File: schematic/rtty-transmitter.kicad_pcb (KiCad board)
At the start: 2 copper layers, 120 x 60 mm, 75 parts, among them J1 USB Type B Connector, J2 USBasp header, J3 2x5 Pin Header Connector Fema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, J4 Conn_01x02_Pin, J5 Conn_01x02_Pin, J6 Conn_01x02_Pin, J7 SMA Vertical Female, Q1 PN2222A, Q2 PN2222A, U1 MCP2221AxP, U2 ATmega328P-P, U3 MCP4901, U4 25LC1024, U5 MCP6022, Y1 16 MHz

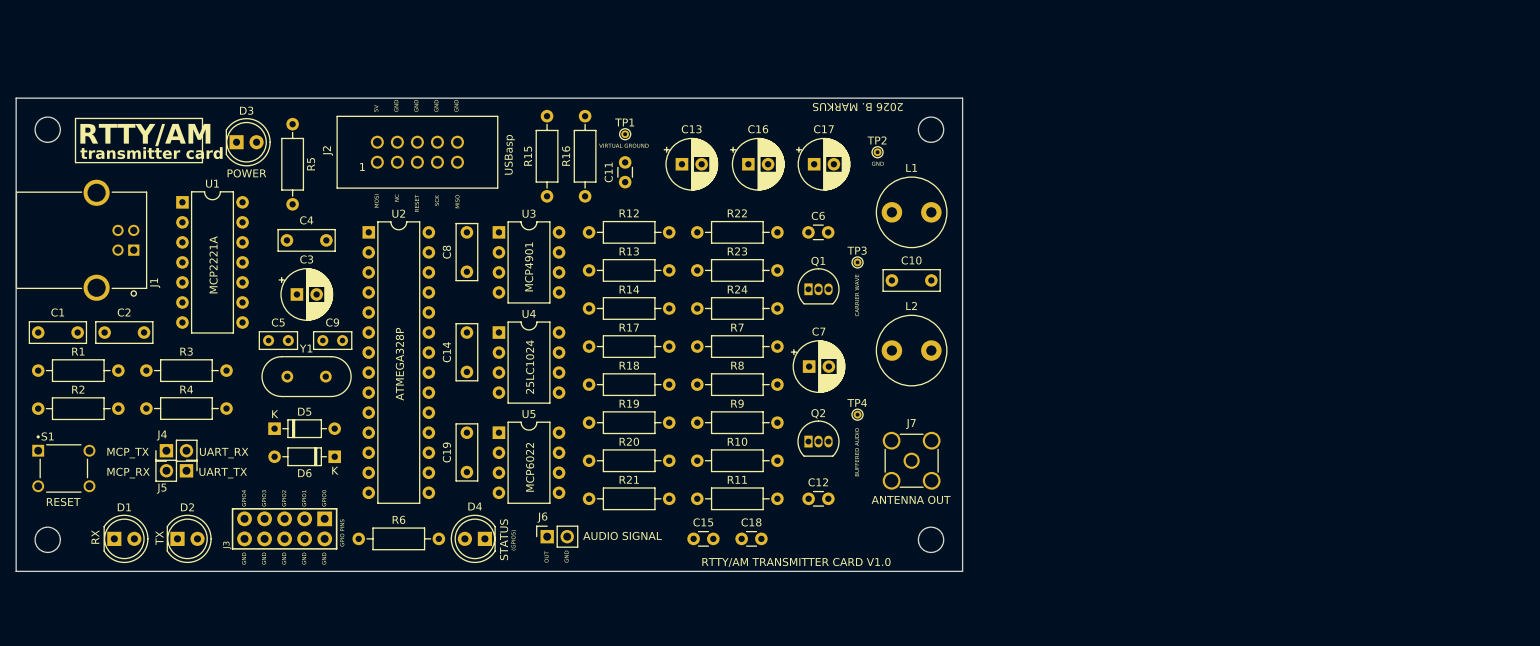
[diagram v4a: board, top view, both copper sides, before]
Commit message: PCB: Ground plane fill zones added
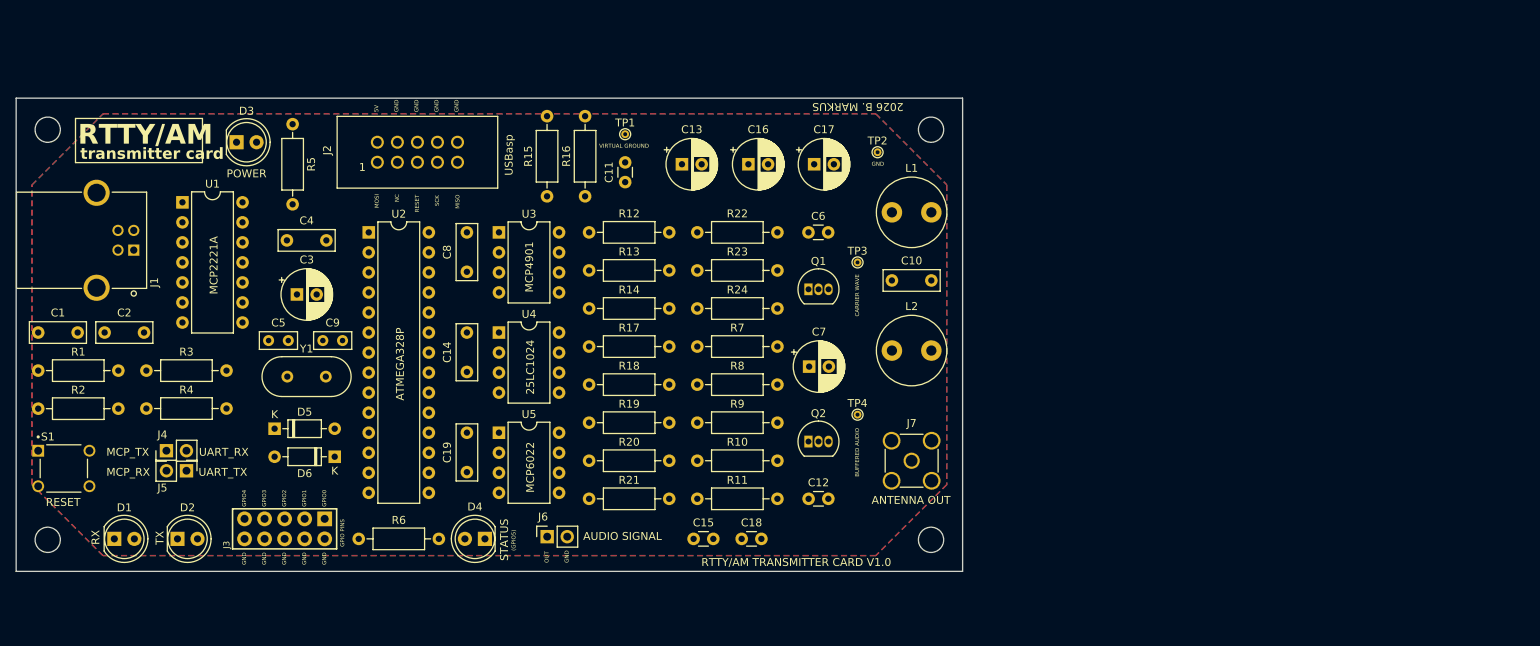
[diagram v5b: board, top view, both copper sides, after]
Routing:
- added copper zone on B.Cu, net GND
- added copper zone on F.Cu, net GND
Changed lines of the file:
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@@
+    )
+  )
+  (zone (net 2) (net_name "GND") (layers "F&B.Cu") (hatch edge 0.5)
+    (connect_pads (clearance 0.5))
+    (min_thickness 0.25) (filled_areas_thickness no)
+    (fill (thermal_gap 0.5) (thermal_bridge_width 0.5))
+    (polygon
+      (pts
+        (xy 2 11)
+        (xy 11 2)
+        (xy 109 2)
+        (xy 118 11)
+        (xy 118 49)
+        (xy 109 58)
+        (xy 11 58)
+        (xy 2 49)
+      )
     )
   )

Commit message: PCB: Routing started
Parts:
- moved C14 5.00 mm to (57.1, 29.7), turned to -90 degrees
- moved C10 5.00 mm to (116.0, 23.1), turned to 180 degrees
- moved C19 5.00 mm to (57.1, 42.4), turned to -90 degrees
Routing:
- net MOSI: track 0.00 -> 69.5 mm
- net Net-(C10-Pad2): track 0.00 -> 32.1 mm
- net SCK: track 0.00 -> 24.2 mm
- net RESET: track 0.00 -> 20.2 mm
- net +5V: track 0.00 -> 19.3 mm
- net Net-(J7-In): track 0.00 -> 15.0 mm
- net Net-(Q1-C): track 0.00 -> 8.64 mm
- net Net-(U2-XTAL1/PB6): track 0.00 -> 5.56 mm
- net Net-(U2-XTAL2/PB7): track 0.00 -> 4.73 mm
- net Net-(D5-K): track 0.00 -> 3.56 mm
- net Net-(D5-A): track 0.00 -> 3.56 mm
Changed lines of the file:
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@@
   )
   (footprint "StockLib:C_100nF_L7.0mm_W2.5mm_P5.00mm" (layer "F.Cu")
-    (at 111.038 23.114)
+    (at 116.038 23.114 180)
     (descr "C, Rect series, Radial, pin pitch=5.00mm, , length*width=7*2.5mm^2, Capacitor")
     (tags "C Rect series Radial pin pitch 5.00mm  length 7mm width 2.5mm Capacitor")
@@
     (property "ki_keywords" "cap capacitor")
     (attr through_hole)
-    (fp_text reference "C10" (at 2.5 -2.5) (layer "F.SilkS")
+    (fp_text reference "C10" (at 2.5 2.54) (layer "F.SilkS")
         (effects (font (size 1 1) (thickness 0.15)))
     )
@@
     (fp_line (start 6 1.25) (end 6 -1.25)
       (stroke (width 0.1) (type solid)) (layer "F.Fab"))
-    (pad "1" thru_hole circle (at 0 0) (size 1.6 1.6) (drill 0.8) (layers "*.Cu" "*.Mask")
+    (pad "1" thru_hole circle (at 0 0 180) (size 1.6 1.6) (drill 0.8) (layers "*.Cu" "*.Mask")
       (net 36 "Net-(Q1-C)") (pintype "passive"))
-    (pad "2" thru_hole circle (at 5 0) (size 1.6 1.6) (drill 0.8) (layers "*.Cu" "*.Mask")
+    (pad "2" thru_hole circle (at 5 0 180) (size 1.6 1.6) (drill 0.8) (layers "*.Cu" "*.Mask")
       (net 16 "Net-(C10-Pad2)") (pintype "passive"))
     (model "C:/Users/bazsi/Documents/KiCad/7.0/3dmodels/Cap 100nF.step"
@@
   )
   (footprint "StockLib:C_100nF_L7.0mm_W2.5mm_P5.00mm" (layer "F.Cu")
-    (at 57.15 34.718 90)
+    (at 57.15 29.718 -90)
     (descr "C, Rect series, Radial, pin pitch=5.00mm, , length*width=7*2.5mm^2, Capacitor")
     (tags "C Rect series Radial pin pitch 5.00mm  length 7mm width 2.5mm Capacitor")
@@
     (property "ki_keywords" "cap capacitor")
     (attr through_hole)
-    (fp_text reference "C14" (at 2.5 -2.5 90) (layer "F.SilkS")
+    (fp_text reference "C14" (at 2.54 2.54 90) (layer "F.SilkS")
         (effects (font (size 1 1) (thickness 0.15)))
     )
@@
     (fp_line (start 6 1.25) (end 6 -1.25)
       (stroke (width 0.1) (type solid)) (layer "F.Fab"))
-    (pad "1" thru_hole circle (at 0 0 90) (size 1.6 1.6) (drill 0.8) (layers "*.Cu" "*.Mask")
+    (pad "1" thru_hole circle (at 0 0 270) (size 1.6 1.6) (drill 0.8) (layers "*.Cu" "*.Mask")
       (net 5 "+5V") (pintype "passive"))
-    (pad "2" thru_hole circle (at 5 0 90) (size 1.6 1.6) (drill 0.8) (layers "*.Cu" "*.Mask")
+    (pad "2" thru_hole circle (at 5 0 270) (size 1.6 1.6) (drill 0.8) (layers "*.Cu" "*.Mask")
       (net 2 "GND") (pintype "passive"))
     (model "C:/Users/bazsi/Documents/KiCad/7.0/3dmodels/Cap 100nF.step"
@@
   )
   (footprint "StockLib:C_100nF_L7.0mm_W2.5mm_P5.00mm" (layer "F.Cu")
-    (at 57.15 47.418 90)
+    (at 57.15 42.418 -90)
     (descr "C, Rect series, Radial, pin pitch=5.00mm, , length*width=7*2.5mm^2, Capacitor")
     (tags "C Rect series Radial pin pitch 5.00mm  length 7mm width 2.5mm Capacitor")
@@
     (property "ki_keywords" "cap capacitor")
     (attr through_hole)
-    (fp_text reference "C19" (at 2.5 -2.5 90) (layer "F.SilkS")
+    (fp_text reference "C19" (at 2.54 2.54 90) (layer "F.SilkS")
         (effects (font (size 1 1) (thickness 0.15)))
     )
@@
     (fp_line (start 6 1.25) (end 6 -1.25)
       (stroke (width 0.1) (type solid)) (layer "F.Fab"))
-    (pad "1" thru_hole circle (at 0 0 90) (size 1.6 1.6) (drill 0.8) (layers "*.Cu" "*.Mask")
+    (pad "1" thru_hole circle (at 0 0 270) (size 1.6 1.6) (drill 0.8) (layers "*.Cu" "*.Mask")
       (net 5 "+5V") (pintype "passive"))
-    (pad "2" thru_hole circle (at 5 0 90) (size 1.6 1.6) (drill 0.8) (layers "*.Cu" "*.Mask")
+    (pad "2" thru_hole circle (at 5 0 270) (size 1.6 1.6) (drill 0.8) (layers "*.Cu" "*.Mask")
       (net 2 "GND") (pintype "passive"))
     (model "C:/Users/bazsi/Documents/KiCad/7.0/3dmodels/Cap 100nF.step"
@@
     )
   )
+  (segment (start 34.38 35.306) (end 32.004 32.93) (width 0.25) (layer "F.Cu") (net 3))
+  (segment (start 32.004 32.93) (end 32.004 30.734) (width 0.25) (layer "F.Cu") (net 3))
+  (segment (start 39.26 35.306) (end 39.26 31.112) (width 0.25) (layer "F.Cu") (net 4))
+  (segment (start 39.26 31.112) (end 38.882 30.734) (width 0.25) (layer "F.Cu") (net 4))
+  (segment (start 7.62 29.718) (end 7.794 29.718) (width 0.5) (layer "F.Cu") (net 5))
+  (segment (start 14.91 19.27) (end 15.02 19.27) (width 0.5) (layer "F.Cu") (net 5))
+  (segment (start 7.62 39.37) (end 2.794 34.544) (width 0.5) (layer "F.Cu") (net 5))
+  (segment (start 2.794 34.544) (end 7.62 29.718) (width 0.5) (layer "F.Cu") (net 5))
+  (segment (start 12.954 39.37) (end 7.62 39.37) (width 0.5) (layer "F.Cu") (net 5))
+  (segment (start 61.214 24.317009) (end 52.0262 15.129209) (width 0.25) (layer "F.Cu") (net 14))
+  (segment (start 44.879991 23.223) (end 51.054 29.397009) (width 0.25) (layer "F.Cu") (net 14))
+  (segment (start 44.238009 23.223) (end 44.879991 23.223) (width 0.25) (layer "F.Cu") (net 14))
+  (segment (start 51.054 43.688) (end 52.324 44.958) (width 0.25) (layer "F.Cu") (net 14))
+  (segment (start 61.214 24.638) (end 61.214 24.317009) (width 0.25) (layer "F.Cu") (net 14))
+  (segment (start 51.352546 6.978) (end 46.9462 6.978) (width 0.25) (layer "F.Cu") (net 14))
+  (segment (start 43.579 10.3452) (end 43.579 22.563991) (width 0.25) (layer "F.Cu") (net 14))
+  (segment (start 46.9462 6.978) (end 45.7962 8.128) (width 0.25) (layer "F.Cu") (net 14))
+  (segment (start 43.579 22.563991) (end 44.238009 23.223) (width 0.25) (layer "F.Cu") (net 14))
+  (segment (start 45.7962 8.128) (end 43.579 10.3452) (width 0.25) (layer "F.Cu") (net 14))
+  (segment (start 51.054 29.397009) (end 51.054 43.688) (width 0.25) (layer "F.Cu") (net 14))
+  (segment (start 52.0262 15.129209) (end 52.0262 7.651654) (width 0.25) (layer "F.Cu") (net 14))
+  (segment (start 52.0262 7.651654) (end 51.352546 6.978) (width 0.25) (layer "F.Cu") (net 14))
+  (segment (start 3.96 39.37) (end 2.794 39.37) (width 0.25) (layer "F.Cu") (net 15))
+  (segment (start 44.704 14.3002) (end 44.704 17.018) (width 0.25) (layer "F.Cu") (net 15))
+  (segment (start 50.8762 8.128) (end 44.704 14.3002) (width 0.25) (layer "F.Cu") (net 15))
+  (segment (start 9.294 44.704) (end 3.96 39.37) (width 0.25) (layer "F.Cu") (net 15))
+  (segment (start 108.458 34.584) (end 111.038 32.004) (width 0.25) (layer "F.Cu") (net 16))
+  (segment (start 111.038 32.004) (end 111.038 23.114) (width 1) (layer "F.Cu") (net 16))
+  (segment (start 106.319 44.958) (end 106.426 44.958) (width 0.25) (layer "F.Cu") (net 16))
+  (segment (start 108.458 42.926) (end 108.458 34.584) (width 0.25) (layer "F.Cu") (net 16))
+  (segment (start 100.477 50.8) (end 106.319 44.958) (width 0.25) (layer "F.Cu") (net 16))
+  (segment (start 106.426 44.958) (end 108.458 42.926) (width 0.25) (layer "F.Cu") (net 16))
+  (segment (start 53.4162 8.128) (end 54.5662 6.978) (width 0.25) (layer "F.Cu") (net 22))
+  (segment (start 54.5662 6.978) (end 60.826 6.978) (width 0.25) (layer "F.Cu") (net 22))
+  (segment (start 62.484 8.636) (end 62.484 20.828) (width 0.25) (layer "F.Cu") (net 22))
+  (segment (start 62.484 20.828) (end 61.214 22.098) (width 0.25) (layer "F.Cu") (net 22))
+  (segment (start 60.826 6.978) (end 62.484 8.636) (width 0.25) (layer "F.Cu") (net 22))
+  (segment (start 116.038 14.478) (end 116.038 23.114) (width 1) (layer "F.Cu") (net 36))
+  (segment (start 32.766 45.466) (end 32.766 41.91) (width 0.25) (layer "F.Cu") (net 44))
+  (segment (start 40.386 41.91) (end 40.386 45.466) (width 0.25) (layer "F.Cu") (net 45))
+  (segment (start 116.038 32.004) (end 113.538 34.504) (width 1) (layer "F.Cu") (net 46))
+  (segment (start 113.538 34.504) (end 113.538 45.974) (width 1) (layer "F.Cu") (net 46))
   (zone (net 2) (net_name "GND") (layers "F&B.Cu") (hatch edge 0.5)
     (connect_pads (clearance 0.5))

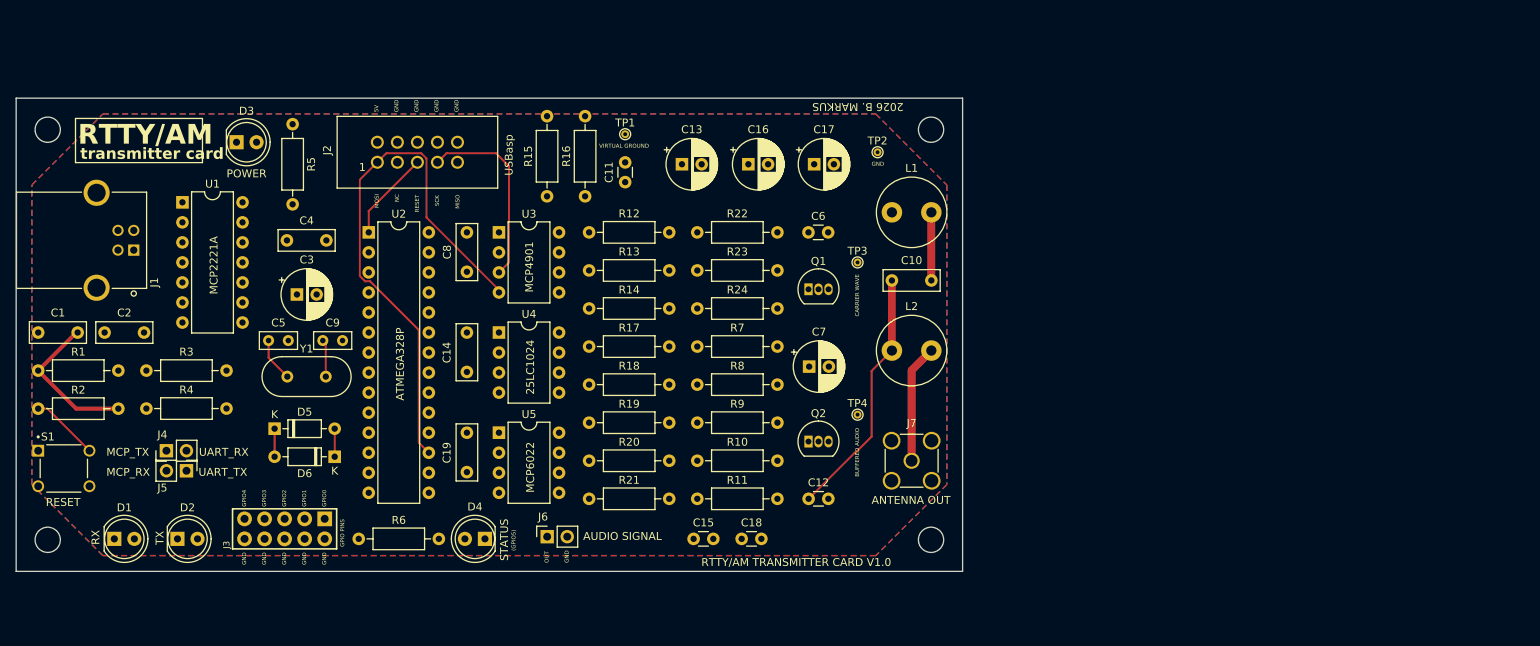
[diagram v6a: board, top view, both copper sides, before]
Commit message: PCB: Routing finished
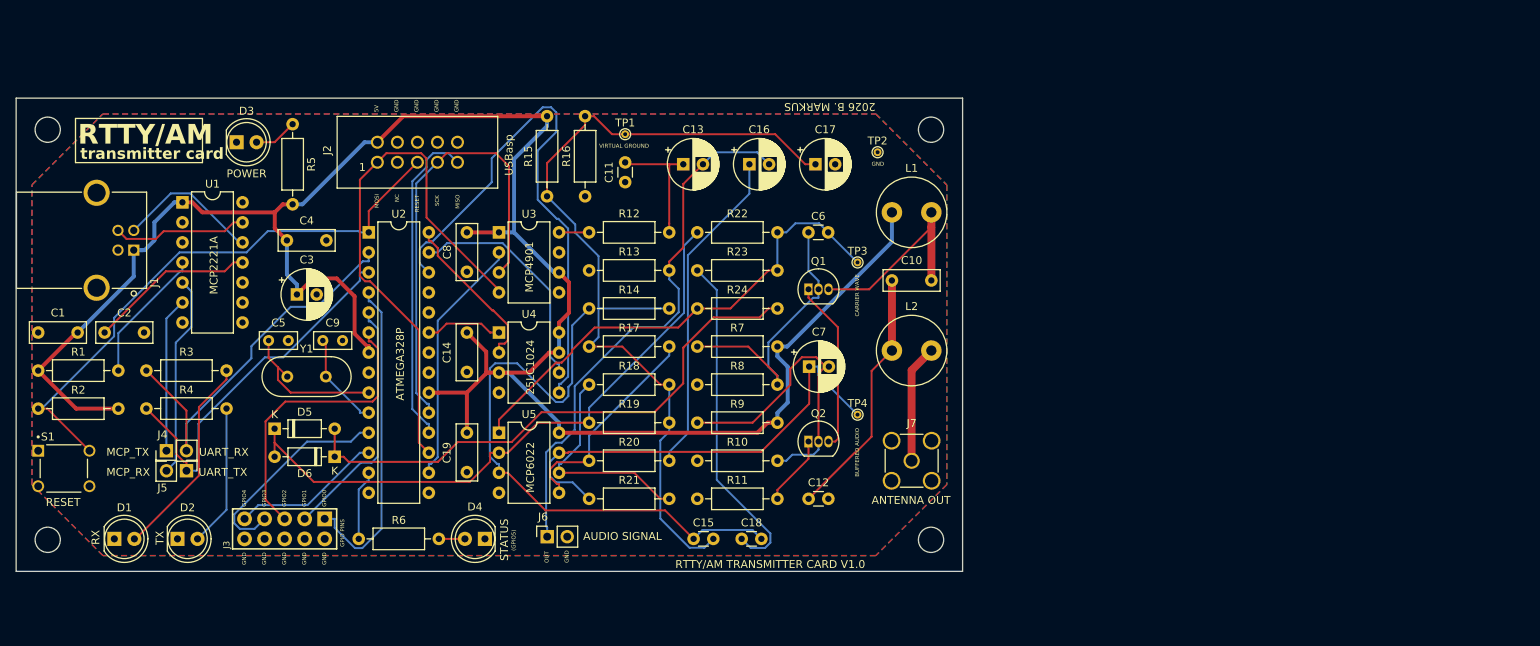
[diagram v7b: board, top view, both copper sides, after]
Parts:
- moved C17 0.17 mm to (101.3, 8.38)
- moved C13 0.17 mm to (84.6, 8.38)
- moved C16 0.13 mm to (93.0, 8.38)
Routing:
- net +5V: track 19.3 -> 269.8 mm
- net VIRTUAL GROUND: track 0.00 -> 113.3 mm
- net Net-(U5A-+): track 0.00 -> 76.3 mm
- net Net-(D5-K): track 3.56 -> 79.1 mm
- net Net-(U2-PC3): track 0.00 -> 69.1 mm
- net AUDIO SIGNAL: track 0.00 -> 68.8 mm
- net Net-(D5-A): track 3.56 -> 70.7 mm
- net CARRIER WAVE: track 0.00 -> 62.5 mm
- net BUFFERED AUDIO: track 0.00 -> 57.9 mm
- net RESET: track 20.2 -> 72.8 mm
- net Net-(J4-Pin_2): track 0.00 -> 49.4 mm
- net Net-(J5-Pin_1): track 0.00 -> 47.7 mm
- net Net-(C18-Pad1): track 0.00 -> 42.8 mm
- net Net-(C16-Pad1): track 0.00 -> 41.8 mm
- net Net-(U2-PD2): track 0.00 -> 41.2 mm
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
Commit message: PCB: PCB layout updated
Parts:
- moved J6 0.28 mm to (67.3, 55.9)
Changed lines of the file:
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@@
   )
   (footprint "Connector_PinSocket_2.54mm:PinSocket_1x02_P2.54mm_Vertical" (layer "F.Cu")
-    (at 67.33 55.601 90)
+    (at 67.33 55.88 90)
     (descr "Through hole straight socket strip, 1x02, 2.54mm pitch, single row (from Kicad 4.0.7), script generated")
     (tags "Through hole socket strip THT 1x02 2.54mm single row")
@@
   (segment (start 84.5821 10.8819) (end 84.5821 18.939) (width 0.25) (layer "F.Cu") (net 6))
   (segment (start 84.5821 18.939) (end 82.804 20.7171) (width 0.25) (layer "F.Cu") (net 6))
-  (segment (start 67.1955 54.2896) (end 67.1955 44.9112) (width 0.25) (layer "B.Cu") (net 6))
-  (segment (start 82.804 21.844) (end 82.804 22.9709) (width 0.25) (layer "B.Cu") (net 6))
+  (segment (start 78.3066 29.0353) (end 82.1056 29.0353) (width 0.25) (layer "B.Cu") (net 6))
+  (segment (start 82.804 22.9709) (end 82.804 21.844) (width 0.25) (layer "B.Cu") (net 6))
   (segment (start 88.606 6.858) (end 93.94 6.858) (width 0.25) (layer "B.Cu") (net 6))
   (segment (start 93.94 6.858) (end 95.464 8.382) (width 0.25) (layer "B.Cu") (net 6))
-  (segment (start 67.33 55.601) (end 67.33 54.4241) (width 0.25) (layer "B.Cu") (net 6))
-  (segment (start 78.3066 29.0353) (end 82.1056 29.0353) (width 0.25) (layer "B.Cu") (net 6))
-  (segment (start 84 24.1669) (end 82.804 22.9709) (width 0.25) (layer "B.Cu") (net 6))
-  (segment (start 87.082 8.382) (end 88.606 6.858) (width 0.25) (layer "B.Cu") (net 6))
-  (segment (start 84 27.1409) (end 84 24.1669) (width 0.25) (layer "B.Cu") (net 6))
-  (segment (start 69.1882 43.688) (end 70.8192 42.057) (width 0.25) (layer "B.Cu") (net 6))
-  (segment (start 70.8192 36.5227) (end 78.3066 29.0353) (width 0.25) (layer "B.Cu") (net 6))
-  (segment (start 70.8192 42.057) (end 70.8192 36.5227) (width 0.25) (layer "B.Cu") (net 6))
   (segment (start 82.1056 29.0353) (end 84 27.1409) (width 0.25) (layer "B.Cu") (net 6))
+  (segment (start 70.8192 42.057) (end 70.8192 36.5227) (width 0.25) (layer "B.Cu") (net 6))
+  (segment (start 67.1955 54.2896) (end 67.1955 44.9112) (width 0.25) (layer "B.Cu") (net 6))
   (segment (start 67.33 54.4241) (end 67.1955 54.2896) (width 0.25) (layer "B.Cu") (net 6))
   (segment (start 67.1955 44.9112) (end 68.4187 43.688) (width 0.25) (layer "B.Cu") (net 6))
+  (segment (start 87.082 8.382) (end 88.606 6.858) (width 0.25) (layer "B.Cu") (net 6))
+  (segment (start 67.33 55.88) (end 67.33 54.4241) (width 0.25) (layer "B.Cu") (net 6))
   (segment (start 68.4187 43.688) (end 69.1882 43.688) (width 0.25) (layer "B.Cu") (net 6))
+  (segment (start 70.8192 36.5227) (end 78.3066 29.0353) (width 0.25) (layer "B.Cu") (net 6))
+  (segment (start 69.1882 43.688) (end 70.8192 42.057) (width 0.25) (layer "B.Cu") (net 6))
+  (segment (start 84 27.1409) (end 84 24.1669) (width 0.25) (layer "B.Cu") (net 6))
+  (segment (start 84 24.1669) (end 82.804 22.9709) (width 0.25) (layer "B.Cu") (net 6))
   (segment (start 23.1724 47.853) (end 23.1724 39.1685) (width 0.25) (layer "F.Cu") (net 7))
   (segment (start 15.1454 55.88) (end 23.1724 47.853) (width 0.25) (layer "F.Cu") (net 7))
